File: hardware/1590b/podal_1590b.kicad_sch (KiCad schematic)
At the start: 56 parts, among them J1 Guitar in, J2 fsw pin 1, J3 fsw pin 2, J4 fsw pin 4, J5 fsw pin 5, J6 fsw pin 6, J7 Left out, J8 Right out, J9 fsw pin 3, SW1 Switch 1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

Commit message: Add footprint for the LM7805
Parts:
- U2: footprint Package_TO_SOT_THT:TO-92_Inline_Wide_78L05_dc -> Library:TO-92_Inline_Wide_78L05_dc
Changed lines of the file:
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@@
 			)
 		)
-		(property "Footprint" "Package_TO_SOT_THT:TO-92_Inline_Wide_78L05_dc"
+		(property "Footprint" "Library:TO-92_Inline_Wide_78L05_dc"
 			(at 90.805 155.575 0)
 			(effects

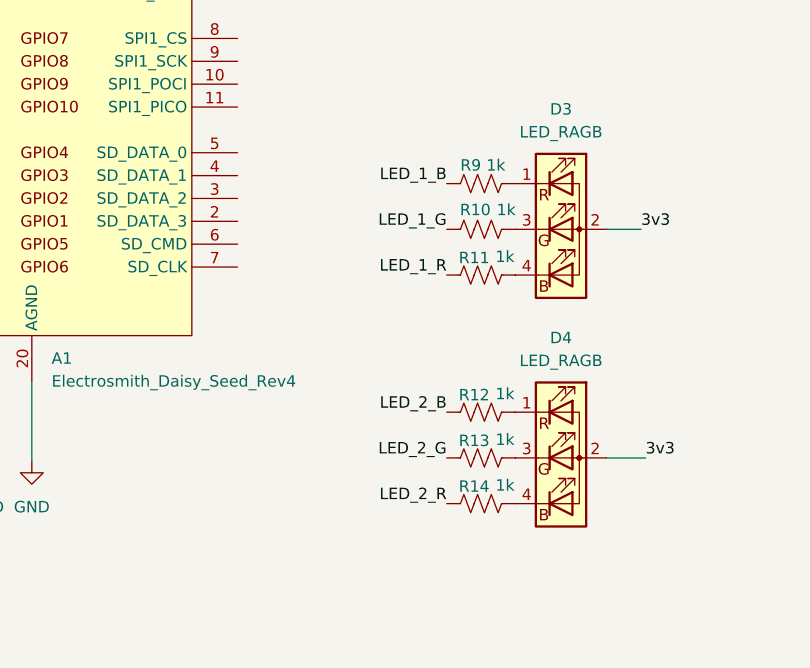
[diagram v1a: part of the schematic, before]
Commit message: Fix Red and blue LEDs - were the wrong way round
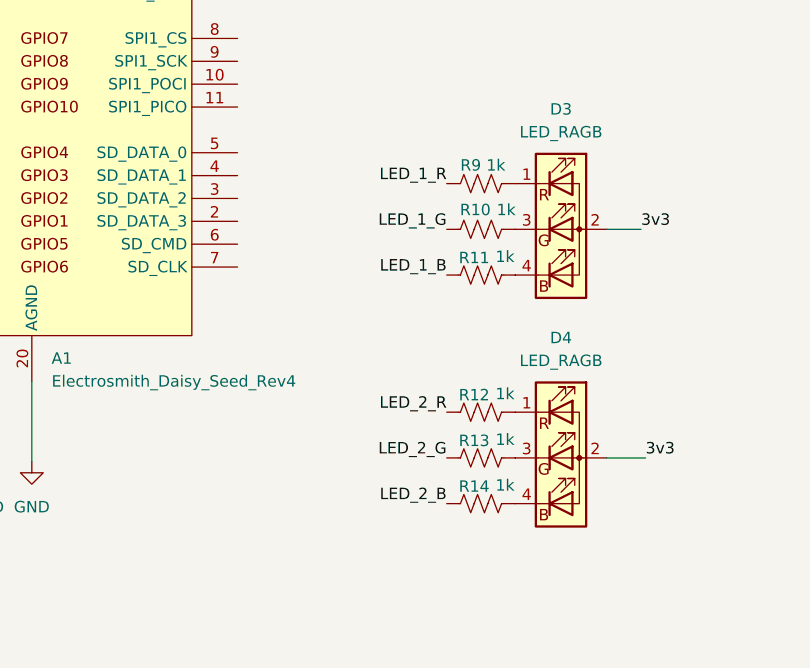
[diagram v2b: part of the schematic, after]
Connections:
- net LED_1_B: now also R11.1; no longer R9.1
- net LED_1_R: now also R9.1; no longer R11.1
- net LED_2_B: now also R14.1; no longer R12.1
- net LED_2_R: now also R12.1; no longer R14.1
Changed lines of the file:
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@@
-		)
-	)
-	(label "LED_2_B"
-		(at 211.201 146.939 180)
-		(fields_autoplaced yes)
-		(effects
-			(font
-				(size 1.27 1.27)
-			)
-			(justify right bottom)
 		)
 	)
@@
 		)
 	)
-	(label "LED_2_R"
+	(label "LED_2_B"
 		(at 211.201 157.099 180)
 		(fields_autoplaced yes)
@@
 		)
 	)
+	(label "LED_1_R"
+		(at 211.201 121.539 180)
+		(fields_autoplaced yes)
+		(effects
+			(font
+				(size 1.27 1.27)
+			)
+			(justify right bottom)
+		)
+	)
 	(label "Left in"
 		(at 120.65 82.55 180)
@@
 		)
 	)
+	(label "LED_1_B"
+		(at 211.201 131.699 180)
+		(fields_autoplaced yes)
+		(effects
+			(font
+				(size 1.27 1.27)
+			)
+			(justify right bottom)
+		)
+	)
 	(label "ENC_CLICK"
 		(at 199.39 90.17 0)
@@
 		)
 	)
+	(label "LED_2_R"
+		(at 211.201 146.939 180)
+		(fields_autoplaced yes)
+		(effects
+			(font
+				(size 1.27 1.27)
+			)
+			(justify right bottom)
+		)
+	)
 	(label "LED_1_G"
 		(at 211.201 126.619 180)
@@
 		)
 	)
-	(label "LED_1_R"
-		(at 211.201 131.699 180)
-		(fields_autoplaced yes)
-		(effects
-			(font
-				(size 1.27 1.27)
-			)
-			(justify right bottom)
-		)
-	)
 	(label "3v3"
 		(at 100.33 102.87 0)
@@
 		)
 	)
-	(label "LED_1_B"
-		(at 211.201 121.539 180)
-		(fields_autoplaced yes)
-		(effects
-			(font
-				(size 1.27 1.27)
-			)
-			(justify right bottom)
-		)
-	)
